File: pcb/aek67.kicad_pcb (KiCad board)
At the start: 2 copper layers, 304.8 x 100.4 mm, 154 parts, among them J1 AVR-ISP-6, K1 K_GRV, K10 K_9, K11 K_0, K12 K_MINUS, K13 K_EQUAL, K14 K_BACKSPACE, K15 K_PAGE_UP, K16 K_TAB, K17 K_Q, K18 K_W, K19 K_E, K2 K_1, K20 K_R, K21 K_T, K22 K_Y, K23 K_U, K24 K_I, K25 K_O, K26 K_P, K27 K_LBRC, K28 K_RBRC, K29 K_BSLSH, K3 K_2, K30 K_PAGE_DN, K31 K_CAPS_LOCK, K32 K_A, K33 K_S, K34 K_D, K35 K_F, K36 K_G, K37 K_H, K38 K_J, K39 K_K, K4 K_3, K40 K_L, K41 K_SEMIC, K42 K_QUOTE, K43 K_ENTER, K44 K_INSERT, K45 K_LSHIFT, K46 K_Z, K47 K_X, K48 K_C, K49 K_V, K5 K_4, K50 K_B, K51 K_N, K52 K_M, K53 K_COMMA, K54 K_DOT, K55 K_SLASH, K56 K_RSHIFT, K57 K_UP, K58 K_DELETE, K59 K_LCTRL, K6 K_5, K60 K_LAPP, K61 K_LALT, K62 K_SPC, K63 K_RALT, K64 K_RAPP, K65 K_LEFT, K66 K_DOWN, K67 K_RIGHT, K7 K_6, K8 K_7, K9 K_8, SW1 SW_PUSH, U1 ATmega32U4-AU, U2 PRTR5V0U2X, X1 XTAL_GND

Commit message: reorder rows/cols to MCU pins
to better orient them
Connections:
- D16 pad 1: row1 -> SCLK
- D17 pad 1: row1 -> SCLK
- D18 pad 1: row1 -> SCLK
- D19 pad 1: row1 -> SCLK
- D20 pad 1: row1 -> SCLK
- D21 pad 1: row1 -> SCLK
- D22 pad 1: row1 -> SCLK
- D23 pad 1: row1 -> SCLK
- D24 pad 1: row1 -> SCLK
- D25 pad 1: row1 -> SCLK
- D26 pad 1: row1 -> SCLK
- D27 pad 1: row1 -> SCLK
- D28 pad 1: row1 -> SCLK
- D29 pad 1: row1 -> SCLK
- D30 pad 1: row1 -> SCLK
- K17 pad 1: SCLK -> col1
- K2 pad 1: SCLK -> col1
- K32 pad 1: SCLK -> col1
- K46 pad 1: SCLK -> col1
- K60 pad 1: SCLK -> col1
- U1 pad 12: row1 -> Net-(U1-Pad12)
- U1 pad 18: col2 -> col0
- U1 pad 19: col3 -> col1
- U1 pad 20: col4 -> col2
- U1 pad 21: col5 -> col3
- U1 pad 22: col7 -> col4
- U1 pad 25: col6 -> col5
- U1 pad 26: col8 -> col6
- U1 pad 27: col9 -> col7
- U1 pad 28: row4 -> col8
- U1 pad 29: row3 -> col9
- U1 pad 30: row2 -> col10
- U1 pad 31: row0 -> col11
- U1 pad 32: Net-(U1-Pad32) -> col12
- U1 pad 36: Net-(U1-Pad36) -> col14
- U1 pad 37: col14 -> col13
- U1 pad 38: col13 -> row2
- U1 pad 39: col12 -> row3
- U1 pad 40: col11 -> row4
- U1 pad 41: col10 -> Net-(U1-Pad41)
- U1 pad 8: col0 -> row0
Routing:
- net row1: track 405.2 -> 0.00 mm, vias 15 -> 0
- net row4: track 0.00 -> 335.1 mm, vias 0 -> 7
- net SCLK: track 94.1 -> 405.2 mm, vias 0 -> 15
- net col1: track 0.00 -> 94.1 mm

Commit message: routed rows
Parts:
- moved J1 7.59 mm to (139.2, 106.4), turned to 90 degrees
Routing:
- net row0: track 378.1 -> 488.5 mm, vias 16 -> 2
- net row2: track 373.0 -> 428.4 mm, vias 14 -> 4
- net row3: track 381.3 -> 414.3 mm, vias 14 -> 2
- net GND: track 178.0 -> 147.5 mm, vias 0 -> 2
- net Net-(R3-Pad1): track 92.5 -> 106.7 mm
- net Net-(R2-Pad1): track 91.6 -> 105.7 mm
- net Net-(C7-Pad1): track 0.00 -> 10.2 mm, vias 0 -> 2
- net row4: track 335.1 -> 341.1 mm, vias 7 -> 0
- net SCLK: track 405.2 -> 399.4 mm, vias 15 -> 3
- net RST: track 0.00 -> 4.74 mm
- net +5V: track 84.7 -> 89.2 mm, vias 12 -> 11
- net col0: track 84.1 -> 84.8 mm
- net MISO: track 0.00 -> 0.68 mm

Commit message: routed almost all rows& columns
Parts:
- moved D53 1.77 mm to (215.1, 84.8)
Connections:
- U1 pad 36: col14 -> col13
- U1 pad 37: col13 -> col14
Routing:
- net col0: track 84.8 -> 277.4 mm, vias 0 -> 4
- net col1: track 94.1 -> 255.4 mm, vias 0 -> 2
- net col2: track 90.4 -> 230.0 mm, vias 0 -> 1
- net col3: track 68.4 -> 190.2 mm, vias 0 -> 1
- net col14: track 77.1 -> 180.3 mm, vias 0 -> 1
- net col4: track 69.7 -> 172.6 mm, vias 0 -> 1
- net col5: track 100.4 -> 191.1 mm, vias 0 -> 3
- net col13: track 84.5 -> 168.0 mm, vias 0 -> 1
- net col6: track 67.0 -> 142.2 mm, vias 0 -> 1
- net col7: track 67.0 -> 124.2 mm, vias 0 -> 1
- net col12: track 97.8 -> 151.9 mm, vias 0 -> 1
- net col8: track 67.0 -> 106.6 mm, vias 0 -> 1
- net col11: track 83.8 -> 119.1 mm, vias 0 -> 1
- net col9: track 67.0 -> 90.0 mm, vias 0 -> 1
- net col10: track 89.0 -> 100.9 mm
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
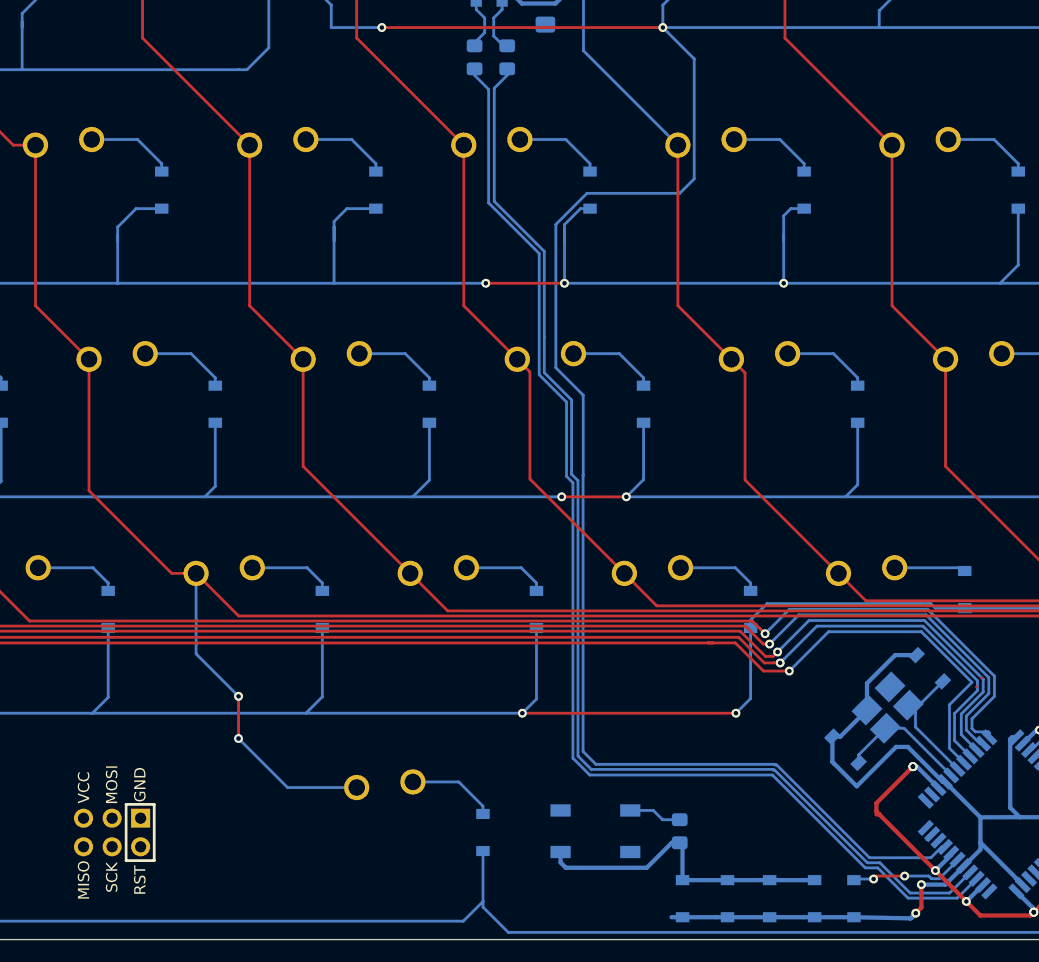
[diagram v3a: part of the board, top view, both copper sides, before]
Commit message: all signals connected
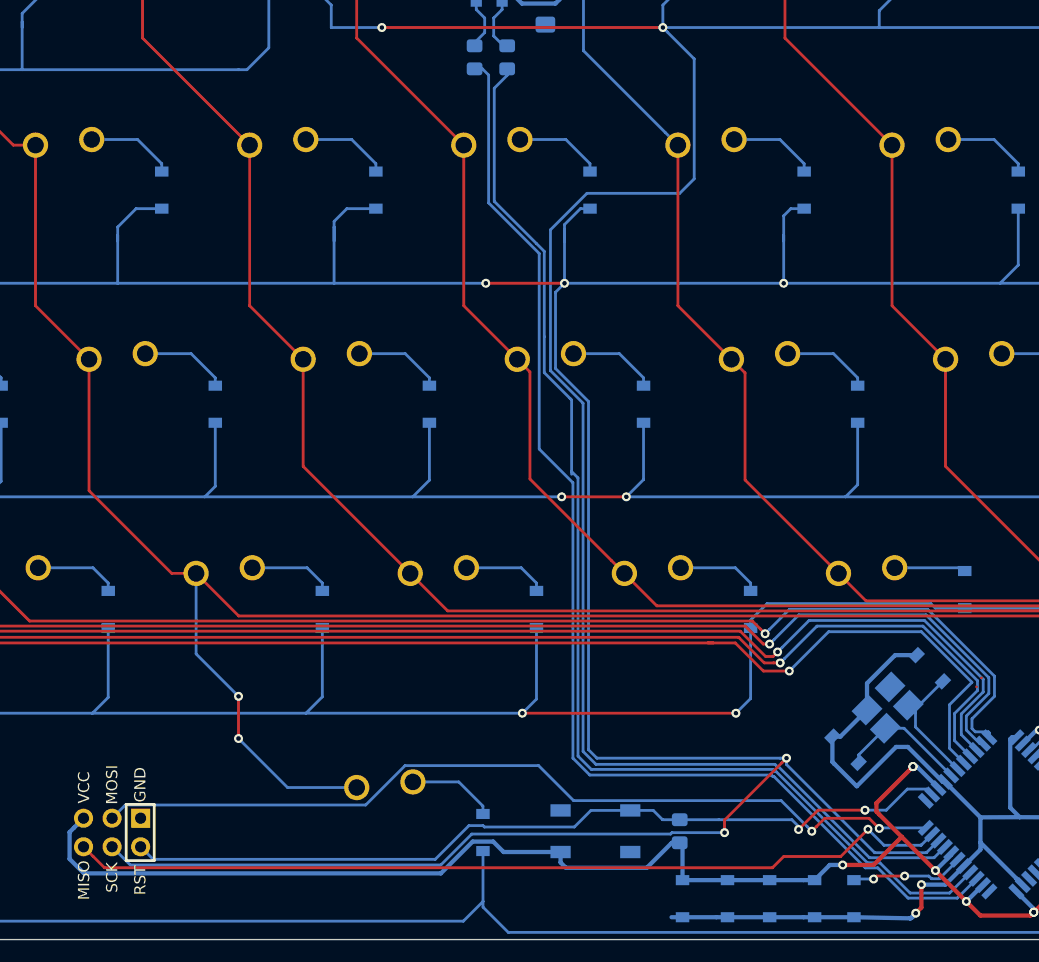
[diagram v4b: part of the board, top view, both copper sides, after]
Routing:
- net SCLK: track 399.4 -> 543.5 mm, vias 3 -> 5
- net MISO: track 0.68 -> 79.4 mm, vias 0 -> 1
- net MOSI: track 0.00 -> 77.6 mm, vias 0 -> 2
- net RST: track 4.74 -> 75.3 mm, vias 0 -> 2
- net +5V: track 88.9 -> 147.9 mm, vias 11 -> 12

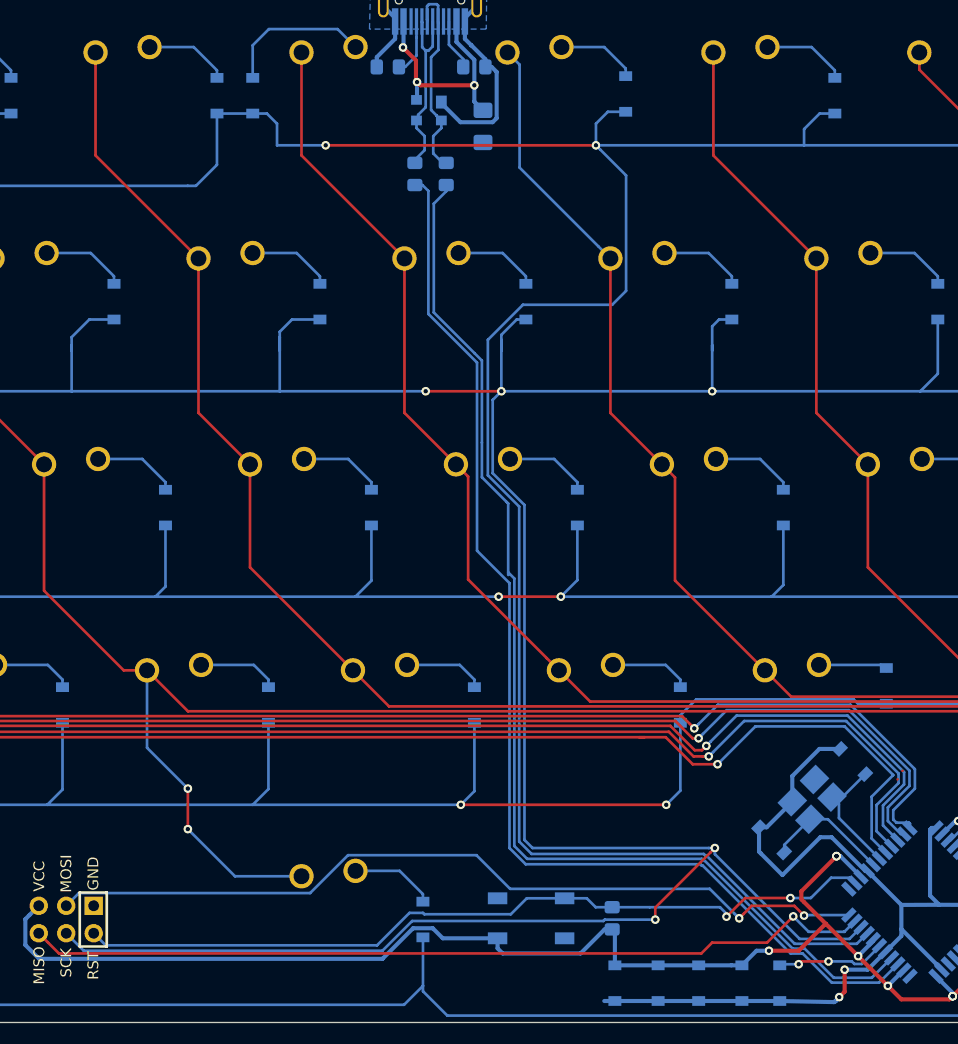
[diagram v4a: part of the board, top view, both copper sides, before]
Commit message: routed GND to MCU
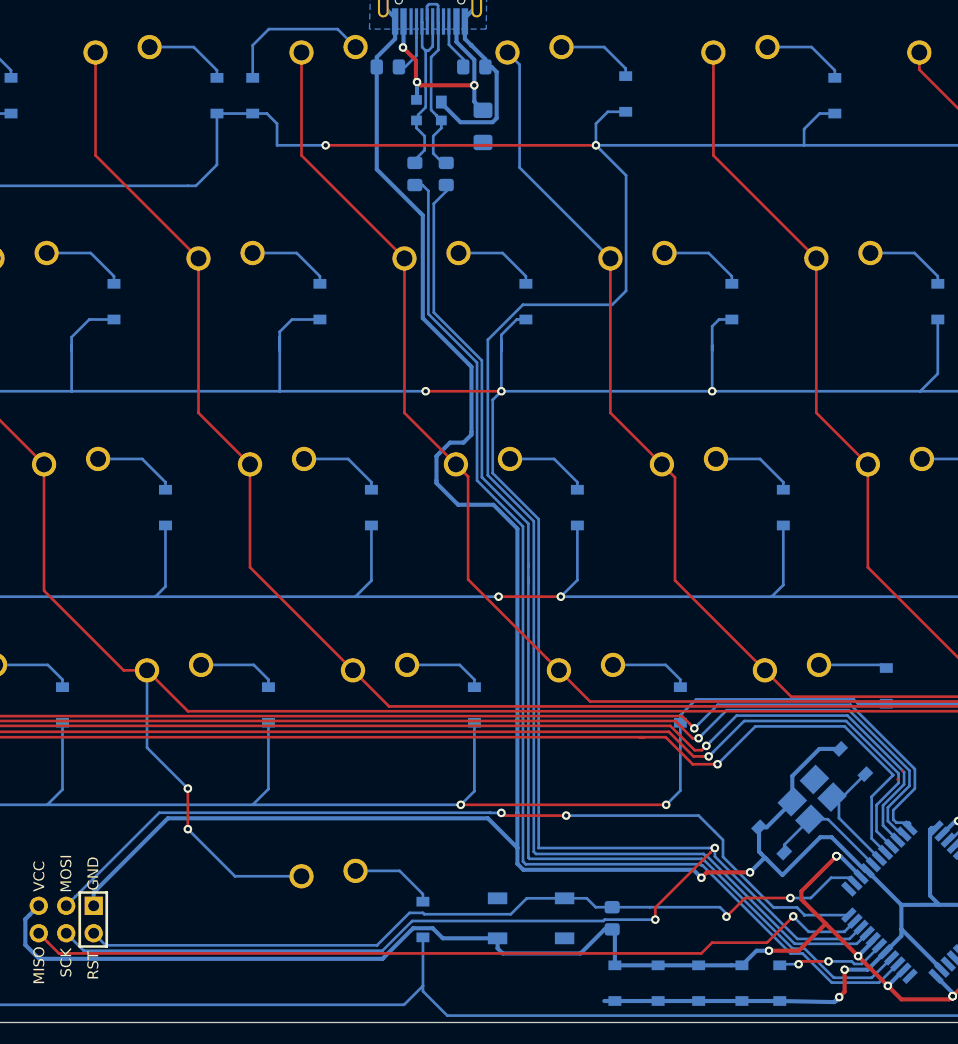
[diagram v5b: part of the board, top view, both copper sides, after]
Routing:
- net GND: track 147.5 -> 300.6 mm, vias 2 -> 4
- net MOSI: track 77.6 -> 80.9 mm

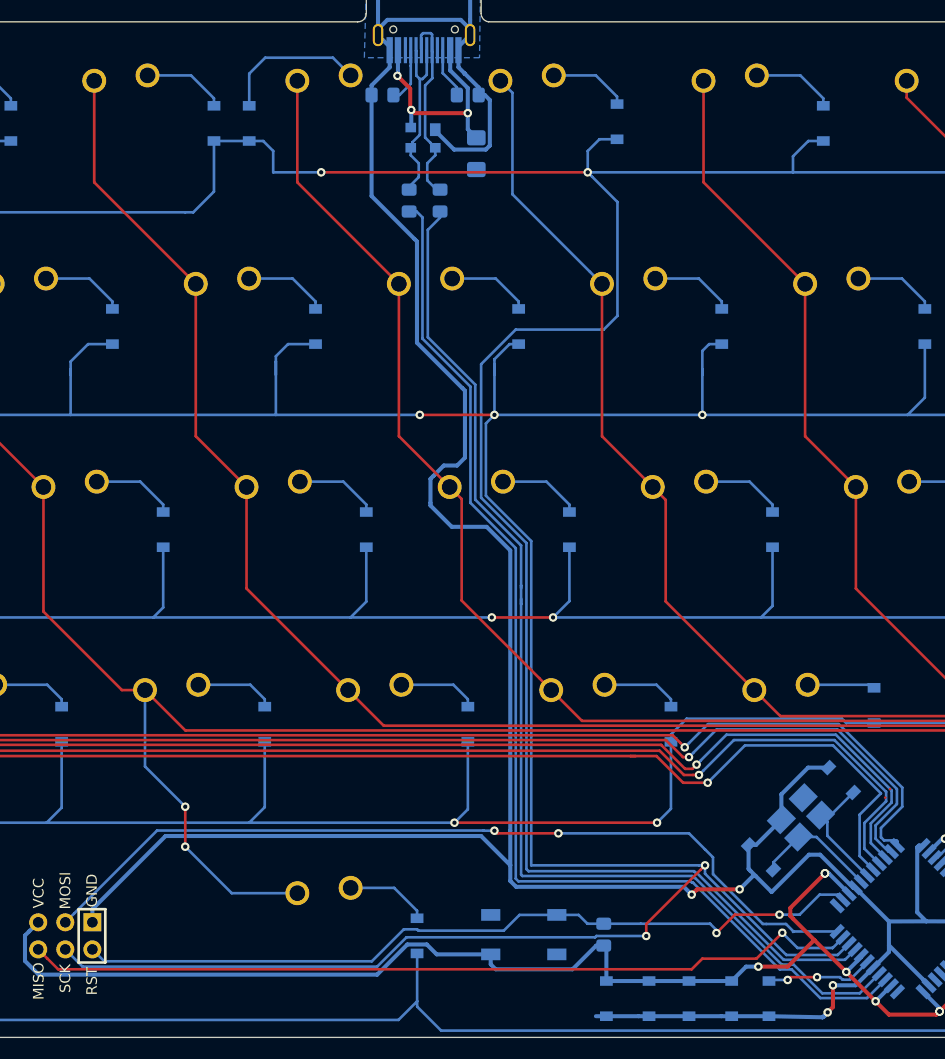
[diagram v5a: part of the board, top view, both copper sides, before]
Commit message: routed +5V
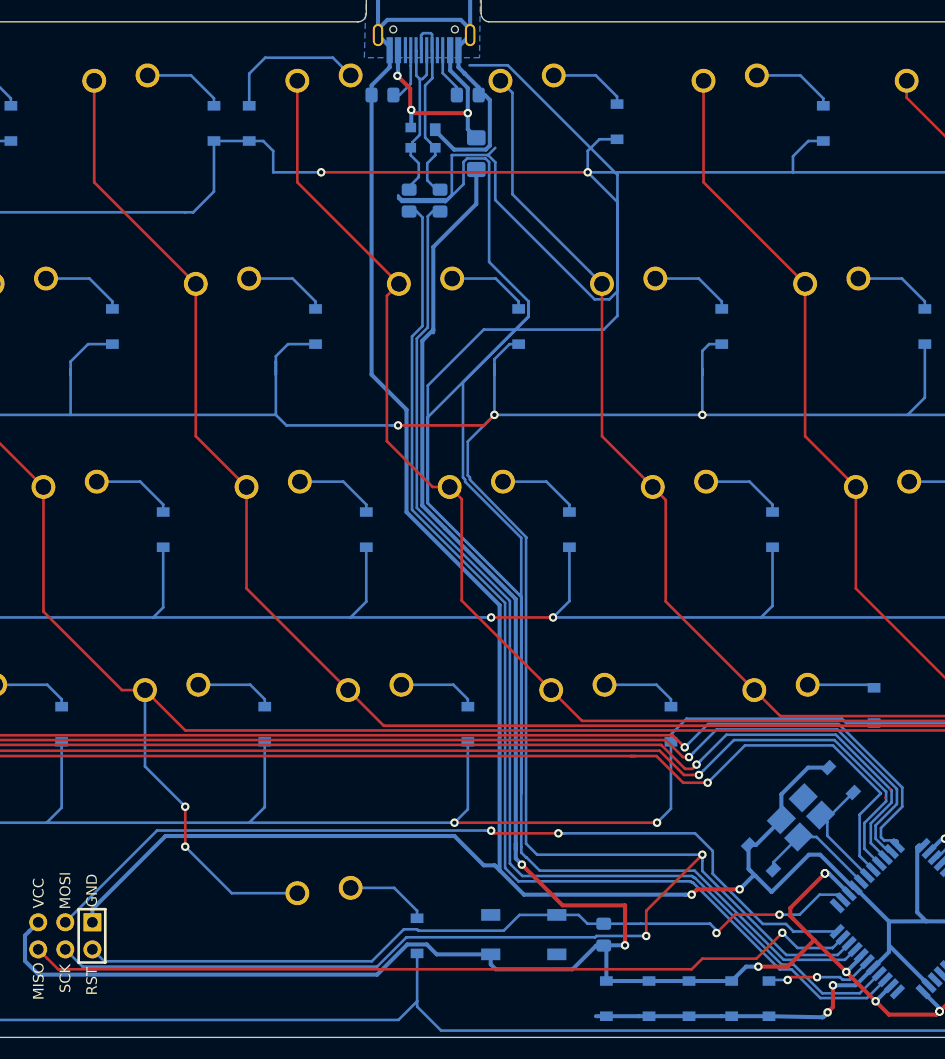
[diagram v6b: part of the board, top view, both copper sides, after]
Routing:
- net row0: track 488.6 -> 670.3 mm
- net +5V: track 147.9 -> 236.9 mm, vias 12 -> 14
- net GND: track 300.6 -> 294.5 mm
- net SCLK: track 543.3 -> 545.9 mm
- net col7: track 124.2 -> 126.1 mm
- net Net-(R3-Pad1): track 107.1 -> 108.0 mm
- net Net-(R2-Pad1): track 106.0 -> 106.5 mm

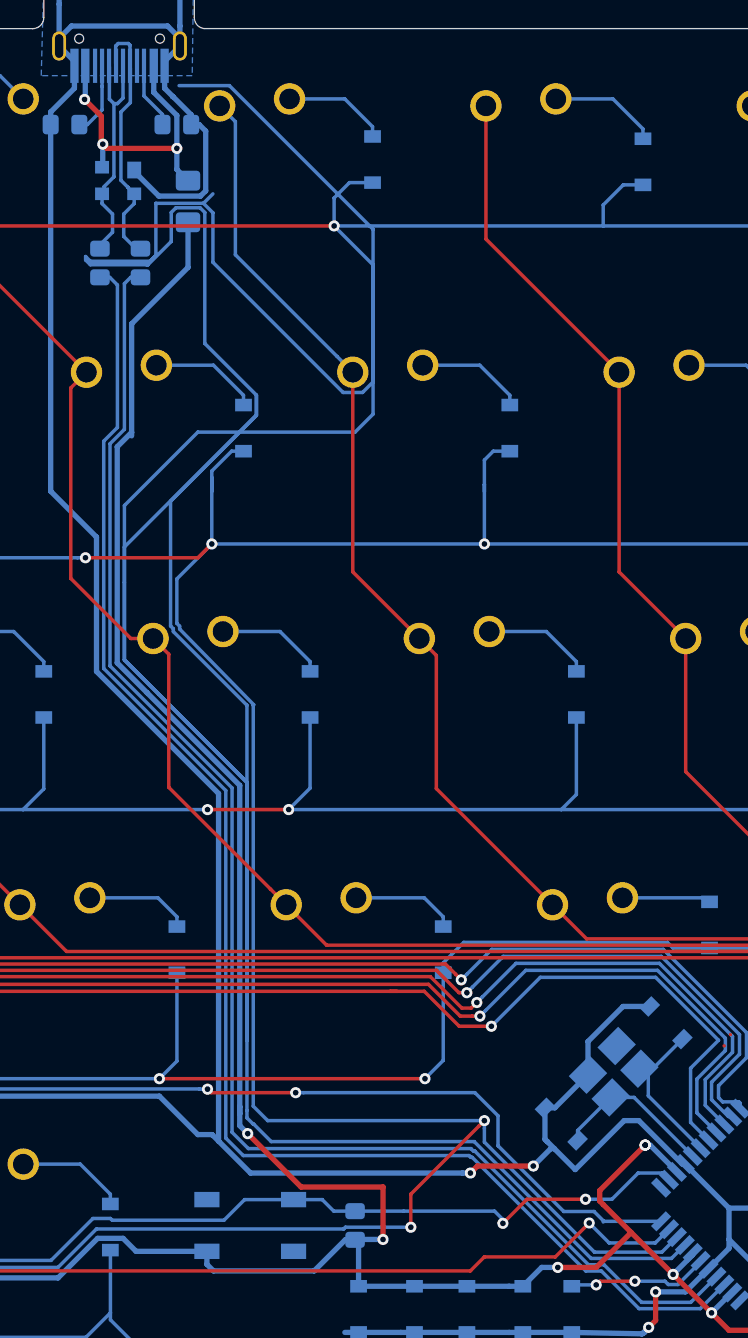
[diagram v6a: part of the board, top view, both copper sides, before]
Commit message: remove row0 multiple tracks
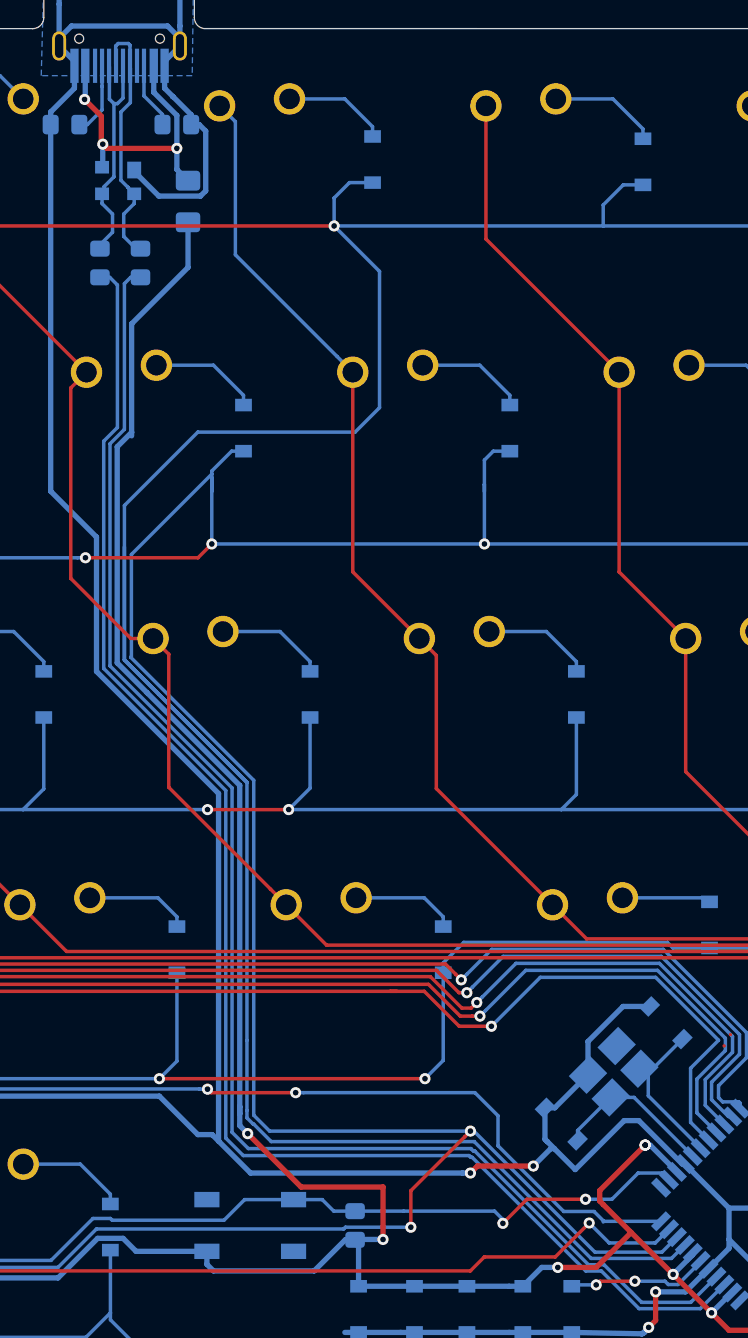
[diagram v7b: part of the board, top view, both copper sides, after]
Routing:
- net row0: track 670.3 -> 514.8 mm
- net SCLK: track 545.9 -> 551.9 mm
